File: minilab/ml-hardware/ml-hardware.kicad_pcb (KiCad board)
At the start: 2 copper layers, 36.3 x 38.1 mm, 80 parts, among them J1 Conn_01x08, J10 BE_Skt-10, J11 BE_Skt-10, J12 BE_Skt-10, J13 BE_Skt-10, J14 BE-Cnn-10, J15 BE-Cnn-10, J16 Molex lite-trap, J17 Molex lite-trap, J18 Molex lite-trap, J19 Molex lite-trap, J2 Molex lite-trap, J20 Molex lite-trap, J21 Conn_01x08, J22 Conn_01x02, J3 Molex lite-trap, J4 Molex lite-trap, J5 Molex lite-trap, J6 Jack-DC, J7 Molex lite-trap, J8 BE-Cnn-10, J9 BE-Cnn-10, SW1 SW_Push, SW2 SW_Push, SW3 SW_Push, SW4 SW_Push, SW5 SW_Push, SW6 SW_Push, SW7 SW_Push, SW8 SW_Push, U2 NE555P

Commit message: minilab: cambia jerarquia y agrega pcb
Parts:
- added C10: 10nF, Capacitor_THT:C_Disc_D6.0mm_W2.5mm_P5.00mm, F.Cu at (165.2, 87.7)
- added H1: MountingHole, MountingHole:MountingHole_3.2mm_M3, F.Cu at (132.2, 63.0)
- added H2: MountingHole, MountingHole:MountingHole_3.2mm_M3, F.Cu at (132.2, 104.2)
- added H3: MountingHole, MountingHole:MountingHole_3.2mm_M3, F.Cu at (257.6, 104.2)
- added H4: MountingHole, MountingHole:MountingHole_3.2mm_M3, F.Cu at (257.6, 63.1)
- added H5: MountingHole, MountingHole:MountingHole_3.2mm_M3, F.Cu at (79.1, 88.1)
- added H6: MountingHole, MountingHole:MountingHole_3.2mm_M3, F.Cu at (79.1, 117.1)
- added H7: MountingHole, MountingHole:MountingHole_3.2mm_M3, F.Cu at (102.5, 126.0)
- added H8: MountingHole, MountingHole:MountingHole_3.2mm_M3, F.Cu at (102.4, 79.2)
- added J23: BE_Skt-2_1, Extras:EdgeSocket-2, B.Cu at (194.9, 108.0)
- added J24: BE_Cnn-2_1, Extras:EdgeConn-2, B.Cu at (177.7, 130.7)
- added J25: Molex lite-trap, Extras:104238-0210, B.Cu at (206.4, 60.8)
- J10: value BE_Skt-10 -> WF-0.1; footprint Extras:EdgeSocket-10 -> Connector_Molex:Molex_KK-254_AE-6410-09A_1x09_P2.54mm_Vertical
- J11: value BE_Skt-10 -> BE_Skt-10_3; moved to B.Cu
- J12: value BE_Skt-10 -> BE_Skt-10_1
- J13: value BE_Skt-10 -> BE_Skt-10_2; moved to B.Cu
- J14: value BE-Cnn-10 -> BE-Cnn-10_1
- J15: value BE-Cnn-10 -> BE-Cnn-10_2; moved to B.Cu
- J16, J7: moved to B.Cu
- J6: footprint Connector_BarrelJack:BarrelJack_Horizontal -> Extras:DC_Jack_Vertical-chasis
- J8: value BE-Cnn-10 -> BE-Cnn-10_3
- J9: value BE-Cnn-10 -> WF-0.1; footprint Extras:EdgeConn-10 -> Connector_Molex:Molex_KK-254_AE-6410-09A_1x09_P2.54mm_Vertical; moved to B.Cu
- R20, R27: footprint Resistor_THT:R_Axial_DIN0204_L3.6mm_D1.6mm_P5.08mm_Horizontal -> Resistor_THT:R_Axial_DIN0204_L3.6mm_D1.6mm_P7.62mm_Horizontal
- SW1, SW2, SW3, SW4, SW5, SW6, SW7, SW8: footprint Button_Switch_THT:SW_Push_2P2T_Toggle_CK_PVA2xxH4xxxxxxV2 -> Extras:SPDT_Switch
- U2: footprint Package_DIP:DIP-8_W7.62mm -> Package_DIP:DIP-8_W7.62mm_LongPads
- moved D4 192.6 mm to (76.8, 168.3), turned to 180 degrees
- moved D6 192.6 mm to (76.8, 175.5), turned to 180 degrees
- moved D8 192.5 mm to (76.8, 182.8), turned to 180 degrees
- moved D10 192.5 mm to (76.8, 190.0), turned to 180 degrees
- moved D3 179.3 mm to (76.8, 139.3), turned to 180 degrees
- moved D5 179.3 mm to (76.8, 146.6), turned to 180 degrees
- moved D7 179.2 mm to (76.8, 153.8), turned to 180 degrees
- moved D9 179.2 mm to (76.8, 161.0), turned to 180 degrees
- moved J15 118.3 mm to (104.6, 164.7), turned to 90 degrees
- moved SW6 114.6 mm to (90.4, 120.8)
- moved SW8 111.8 mm to (90.5, 128.0)
- moved R19 109.5 mm to (158.8, 58.4), turned to 180 degrees
- moved J9 107.5 mm to (102.2, 92.4), turned to -90 degrees
- moved SW2 96.1 mm to (90.4, 106.3)
- moved SW4 93.3 mm to (90.4, 113.5)
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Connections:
- C9 pad 1: Net-(U2-TR) -> Net-(U2-THR)
- J10 pad 6: unconnected-(J10-Pin_6-Pad6)_1 -> /Placa Principal/Bi4
- J10 pad 7: /Placa Principal/Bi4 -> /Placa Principal/Bi5
- J10 pad 8: /Placa Principal/Bi5 -> /Placa Principal/Bi6
- J10 pad 9: /Placa Principal/Bi6 -> /Placa Principal/Bi7
- J16 pad 2: (no net) -> /Placa Principal/OSCo
- J7 pad 1: /GND -> /Entrada alimentacion/+Vin
- J7 pad 2: /Placa Principal/+Vin -> /Entrada alimentacion/GND
- J9 pad 6: unconnected-(J9-Pin_6-Pad6) -> /Botones/Bo4
- J9 pad 7: /Botones/Bo4 -> /Botones/Bo5
- J9 pad 8: /Botones/Bo5 -> /Botones/Bo6
- J9 pad 9: /Botones/Bo6 -> /Botones/Bo7
- RV1 pad 3: Net-(U2-TR) -> Net-(U2-THR)
- U2 pad 2: Net-(U2-TR) -> Net-(U2-THR)
- U2 pad 5: unconnected-(U2-CV-Pad5) -> Net-(U2-CV)
- U2 pad 6: unconnected-(U2-THR-Pad6) -> Net-(U2-THR)
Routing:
- net /+5V: track 0.00 -> 256.7 mm, vias 0 -> 2
- net /Placa Principal/Bi3: track 0.00 -> 88.4 mm
- net /Leds/+5V: track 0.00 -> 85.8 mm
- net /Placa Principal/Bi4: track 0.00 -> 83.1 mm
- net /Placa Principal/Bi2: track 0.00 -> 77.7 mm
- net /Salidas/+5V: track 34.4 -> 112.0 mm, vias 0 -> 4
- net /Placa Principal/Bi5: track 0.00 -> 72.7 mm
- net /Entradas/GND: track 14.4 -> 84.4 mm, vias 0 -> 4
- net /Placa Principal/Bi1: track 0.00 -> 67.1 mm
- net /Placa Principal/OSCo: track 0.00 -> 65.3 mm, vias 0 -> 2
- net /Placa Principal/Bi6: track 0.00 -> 62.1 mm
- net /Placa Principal/Ii3: track 0.00 -> 60.2 mm
- net Net-(U2-THR): track 0.00 -> 58.2 mm, vias 0 -> 2
- net /Placa Principal/Bi0: track 0.00 -> 56.2 mm
- net /Placa Principal/Ii4: track 0.00 -> 55.1 mm
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- added copper zone on B.Cu, net (none)
- added copper zone on B.Cu, net /Botones/GND
- added copper zone on B.Cu, net /Entrada alimentacion/GND
- added copper zone on B.Cu, net /Entradas/GND
- added copper zone on B.Cu, net /GND
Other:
- board size 36.3 x 38.1 mm -> 243.3 x 137.8 mm
- board text added: "Inputs PCB Rev.: 1.0"
- board text added: "LEDs PCB Rev.: 1.0"
- board text added: "Outputs PCB Rev.: 1.0"
- board text added: "minilab-pro by fpp"
- board text added: "minilab-pro by fpp Main PCB Rev.: 1.0"

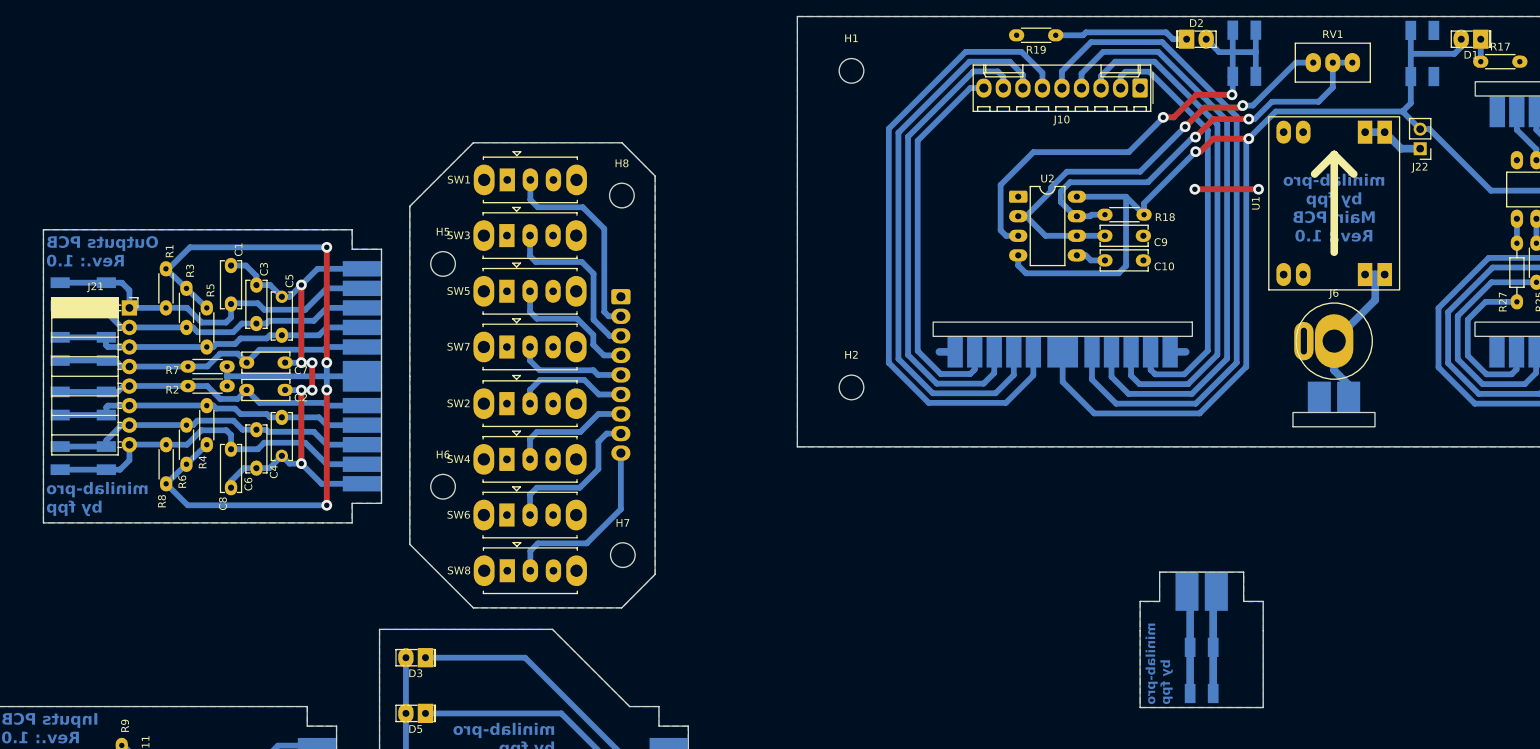
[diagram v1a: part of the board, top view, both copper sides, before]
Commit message: minilab: Agrega 2da opc conectores y modelos 3d
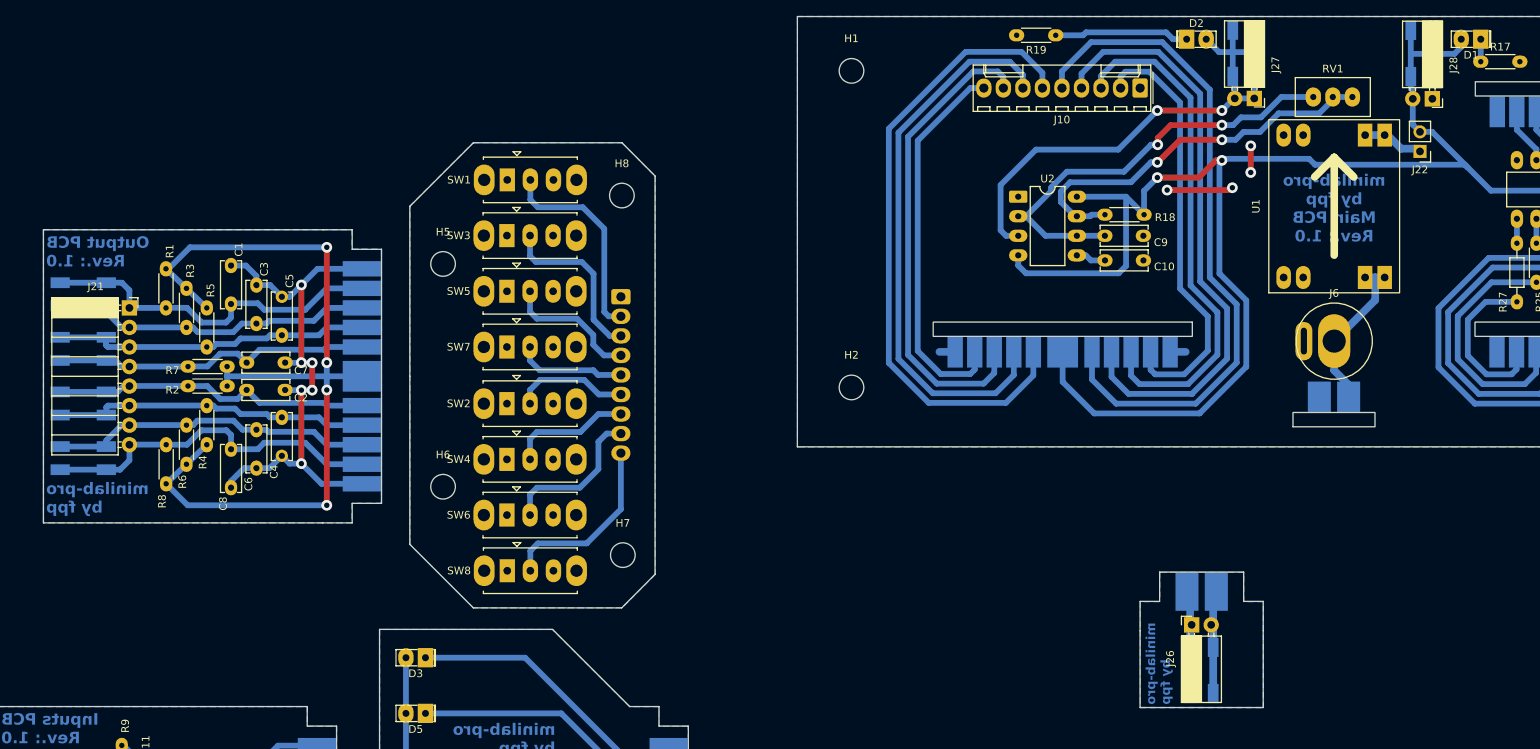
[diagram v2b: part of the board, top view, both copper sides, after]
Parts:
- added J26: Conn_01x02, Connector_PinSocket_2.54mm:PinSocket_1x02_P2.54mm_Horizontal, F.Cu at (176.4, 135.0)
- added J27: Conn_01x02, Connector_PinSocket_2.54mm:PinSocket_1x02_P2.54mm_Horizontal, F.Cu at (184.6, 66.6)
- added J28: Conn_01x02, Connector_PinSocket_2.54mm:PinSocket_1x02_P2.54mm_Horizontal, F.Cu at (207.7, 66.7)
- moved RV1 4.47 mm to (197.3, 66.4)
- moved U1 0.38 mm to (194.9, 80.6)
- moved J22 0.36 mm to (206.1, 73.5)
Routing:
- net /Placa Principal/OSCo: track 65.3 -> 71.6 mm
- net /+5V: track 256.7 -> 261.9 mm
- net /GND: track 12.3 -> 16.1 mm, vias 2 -> 4
- net Net-(U2-DIS): track 54.7 -> 51.1 mm
- net Net-(U2-THR): track 58.2 -> 56.9 mm
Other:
- board text added: "Output PCB Rev.: 1.0"
- board text removed: "Outputs PCB Rev.: 1.0"

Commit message: minilab: Corrige huella molex microfit y edge-*-02
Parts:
- J16, J17, J18, J19, J2, J20, J25, J3, J4, J5, J7: footprint Extras:104238-0210 -> Extras:Molex-Lite_trap
- J6: moved to B.Cu
- moved J26 12.4 mm to (185.6, 126.6)
- moved J7 12.1 mm to (186.9, 133.1), turned to 0 degrees
- moved J24 11.2 mm to (186.9, 124.3)
- moved J17 6.30 mm to (26.9, 88.9), turned to -90 degrees
- moved J18 5.74 mm to (26.9, 97.4), turned to -90 degrees
- moved J20 5.53 mm to (26.9, 114.3), turned to -90 degrees
- moved J19 5.47 mm to (26.9, 105.8), turned to -90 degrees
- moved J2 3.71 mm to (24.7, 178.6), turned to -90 degrees
- moved C2 3.44 mm to (50.3, 103.4)
- moved C7 3.44 mm to (50.3, 99.9)
- moved R2 3.44 mm to (47.8, 102.9)
- moved R5 3.44 mm to (45.1, 92.8)
- moved R7 3.44 mm to (47.8, 100.4)
- moved R8 3.44 mm to (39.9, 115.6)
- moved R4 3.44 mm to (45.1, 110.5)
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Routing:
- net /GND: track 16.1 -> 538.6 mm
- net /Botones/GND: track 0.00 -> 82.3 mm
- net /Salidas/Bi7: track 45.8 -> 56.3 mm
- net /Entradas/I7: track 44.4 -> 55.0 mm
- net /+5V: track 261.9 -> 272.2 mm
- net Net-(U2-THR): track 56.9 -> 65.2 mm
- net Net-(U2-DIS): track 51.1 -> 58.2 mm
- net /Entradas/I0: track 44.6 -> 49.8 mm
- net /Salidas/Bi0: track 45.6 -> 50.6 mm
- net /Entradas/I1: track 42.5 -> 46.7 mm
- net /Salidas/Bi1: track 42.3 -> 46.5 mm
- net /Salidas/Bi6: track 42.3 -> 46.4 mm
- net /Entradas/I6: track 42.5 -> 46.6 mm
- net /Salidas/Bi3: track 41.4 -> 43.9 mm
- net /Salidas/Bi4: track 41.5 -> 43.9 mm
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- removed copper zone on B.Cu, net (none)
- removed copper zone on B.Cu, net /Botones/GND
- removed copper zone on B.Cu, net /Entrada alimentacion/GND
- removed copper zone on B.Cu, net /Entradas/GND
- removed copper zone on B.Cu, net /GND
- removed copper zone on B.Cu, net /Salidas/GND
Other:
- board size 243.3 x 137.8 mm -> 247.2 x 137.8 mm
- board text added: "Inputs PCB Rev.: 1.1"
- board text added: "Outputs PCB Rev.: 1.1"
- board text added: "Rev.: 1.0"
- board text added: "Switches PCB"
- board text added: "minilab-pro by fpp Main PCB Rev.: 1.1"
- board text removed: "Inputs PCB Rev.: 1.0"
- board text removed: "Output PCB Rev.: 1.0"
- board text removed: "minilab-pro by fpp Main PCB Rev.: 1.0"

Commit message: minilab: Actualiza placa de alimentacion
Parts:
- moved J26 7.61 mm to (185.6, 134.2)
- moved J7 7.61 mm to (186.9, 140.8)
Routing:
- net /Entrada alimentacion/+Vin: track 13.4 -> 23.2 mm
- net /Entrada alimentacion/GND: track 13.4 -> 23.2 mm
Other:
- outline, holes or cut-outs redrawn
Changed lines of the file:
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@@
 	(footprint "Connector_PinSocket_2.54mm:PinSocket_1x02_P2.54mm_Horizontal"
 		(layer "F.Cu")
-		(at 185.5724 126.619 90)
+		(at 185.5678 134.2332 90)
 		(descr "Through hole angled socket strip, 1x02, 2.54mm pitch, 8.51mm socket length, single row (from Kicad 4.0.7), script generated")
 		(tags "Through hole angled socket strip THT 1x02 2.54mm single row")
@@
 	(footprint "Extras:Molex-Lite_trap"
 		(layer "B.Cu")
-		(at 186.8978 133.1428)
+		(at 186.8932 140.757)
 		(property "Reference" "J7"
 			(at 5 -3.3 90)
@@
 			(polygon
 				(pts
-					(xy 182.9978 134.1428) (xy 182.9978 128.2428) (xy 183.8978 128.2428) (xy 183.8978 129.2428) (xy 184.2978 129.2428)
-					(xy 184.2978 134.1428)
+					(xy 182.9932 141.757) (xy 182.9932 135.857) (xy 183.8932 135.857) (xy 183.8932 136.857) (xy 184.2932 136.857)
+					(xy 184.2932 141.757)
 				)
 			)
@@
 			(polygon
 				(pts
-					(xy 190.7978 134.1428) (xy 190.7978 128.2428) (xy 189.8978 128.2428) (xy 189.8978 129.2428) (xy 189.4978 129.2428)
-					(xy 189.4978 134.1428)
+					(xy 190.7932 141.757) (xy 190.7932 135.857) (xy 189.8932 135.857) (xy 189.8932 136.857) (xy 189.4932 136.857)
+					(xy 189.4932 141.757)
 				)
 			)
@@
 			(polygon
 				(pts
-					(xy 186.4978 139.8428) (xy 186.4978 134.1428) (xy 185.4978 134.1428) (xy 185.4978 129.2428) (xy 185.8978 129.2428)
-					(xy 185.8978 128.1428) (xy 187.8978 128.1428) (xy 187.8978 129.2428) (xy 188.2978 129.2428) (xy 188.2978 134.1428)
-					(xy 187.2978 134.1428) (xy 187.2978 139.8428)
+					(xy 186.4932 147.457) (xy 186.4932 141.757) (xy 185.4932 141.757) (xy 185.4932 136.857) (xy 185.8932 136.857)
+					(xy 185.8932 135.757) (xy 187.8932 135.757) (xy 187.8932 136.857) (xy 188.2932 136.857) (xy 188.2932 141.757)
+					(xy 187.2932 141.757) (xy 187.2932 147.457)
 				)
 			)
@@
 	(gr_line
 		(start 194.3908 129.3876)
-		(end 194.3862 140.4932)
+		(end 194.3862 148.1582)
 		(stroke
 			(width 0.05)
@@
 	(gr_line
 		(start 179.4048 129.3876)
-		(end 179.4002 140.4932)
+		(end 179.4002 148.1582)
 		(stroke
 			(width 0.05)
@@
 	)
 	(gr_line
-		(start 179.4002 140.4932)
-		(end 194.3862 140.4932)
+		(start 179.4002 148.1582)
+		(end 194.3862 148.1582)
 		(stroke
 			(width 0.05)
@@
 	)
 	(gr_text "minilab-pro\nby fpp"
-		(at 181.2638 140.1122 90)
+		(at 192.2018 127.3556 270)
 		(layer "B.Cu")
 		(effects
@@
 		(layer "User.1")
 		(pts
+			(xy 194.3908 125.5776) (xy 194.3908 148.1328)
+		)
+		(height 7.2598)
+		(orientation 1)
+		(format
+			(prefix "")
+			(suffix "")
+			(units 3)
+			(units_format 0)
+			(precision 4)
+			(suppress_zeroes yes)
+		)
+		(style
+			(thickness 0.1)
+			(arrow_length 1.27)
+			(text_position_mode 0)
+			(arrow_direction outward)
+			(extension_height 0.58642)
+			(extension_offset 0.5)
+			(keep_text_aligned yes)
+		)
+		(gr_text "22,5552"
+			(at 200.5006 136.8552 90)
+			(layer "User.1")
+			(effects
+				(font
+					(size 1 1)
+					(thickness 0.15)
+				)
+			)
+		)
+	)
+	(dimension
+		(type orthogonal)
+		(layer "User.1")
+		(pts
 			(xy 145.6825 99.568) (xy 125.222 99.568)
 		)
@@
 	)
 	(segment
-		(start 185.3978 138.6672)
-		(end 185.3978 125.8302)
+		(start 184.8932 146.857)
+		(end 184.8932 135.157)
+		(width 1)
+		(layer "B.Cu")
+		(net 85)
+	)
+	(segment
+		(start 184.8932 124.4072)
+		(end 184.9928 124.3076)
+		(width 1)
+		(layer "B.Cu")
+		(net 85)
+	)
+	(segment
+		(start 184.8932 135.157)
+		(end 184.8932 124.4072)
 		(width 1)
 		(layer "B.Cu")
@@
 	)
 	(segment
-		(start 188.3978 138.6672)
-		(end 188.3978 125.8302)
+		(start 188.8932 124.398)
+		(end 188.8028 124.3076)
 		(width 1)
 		(layer "B.Cu")
@@
 		(width 1)
 		(layer "B.Cu")
+		(net 86)
+	)
+	(segment
+		(start 188.8932 146.857)
+		(end 188.8932 124.398)
+		(width 1)
+		(layer "B.Cu")
